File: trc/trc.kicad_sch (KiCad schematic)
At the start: 23 parts, among them J1 PWR, J2 Control, J3 Inverter, J4 BMS, J5 States, J6 Relays, SW1 EXT_FAULT_JUMPER

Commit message: docs(trc): update sheet information
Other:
- title: Pre-Charge -> TSAC Relay Controller
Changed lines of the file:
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@@
   (paper "A4")
   (title_block
-    (title "Pre-Charge")
+    (title "TSAC Relay Controller")
     (date "2023-04-27")
     (rev "2.0.0")

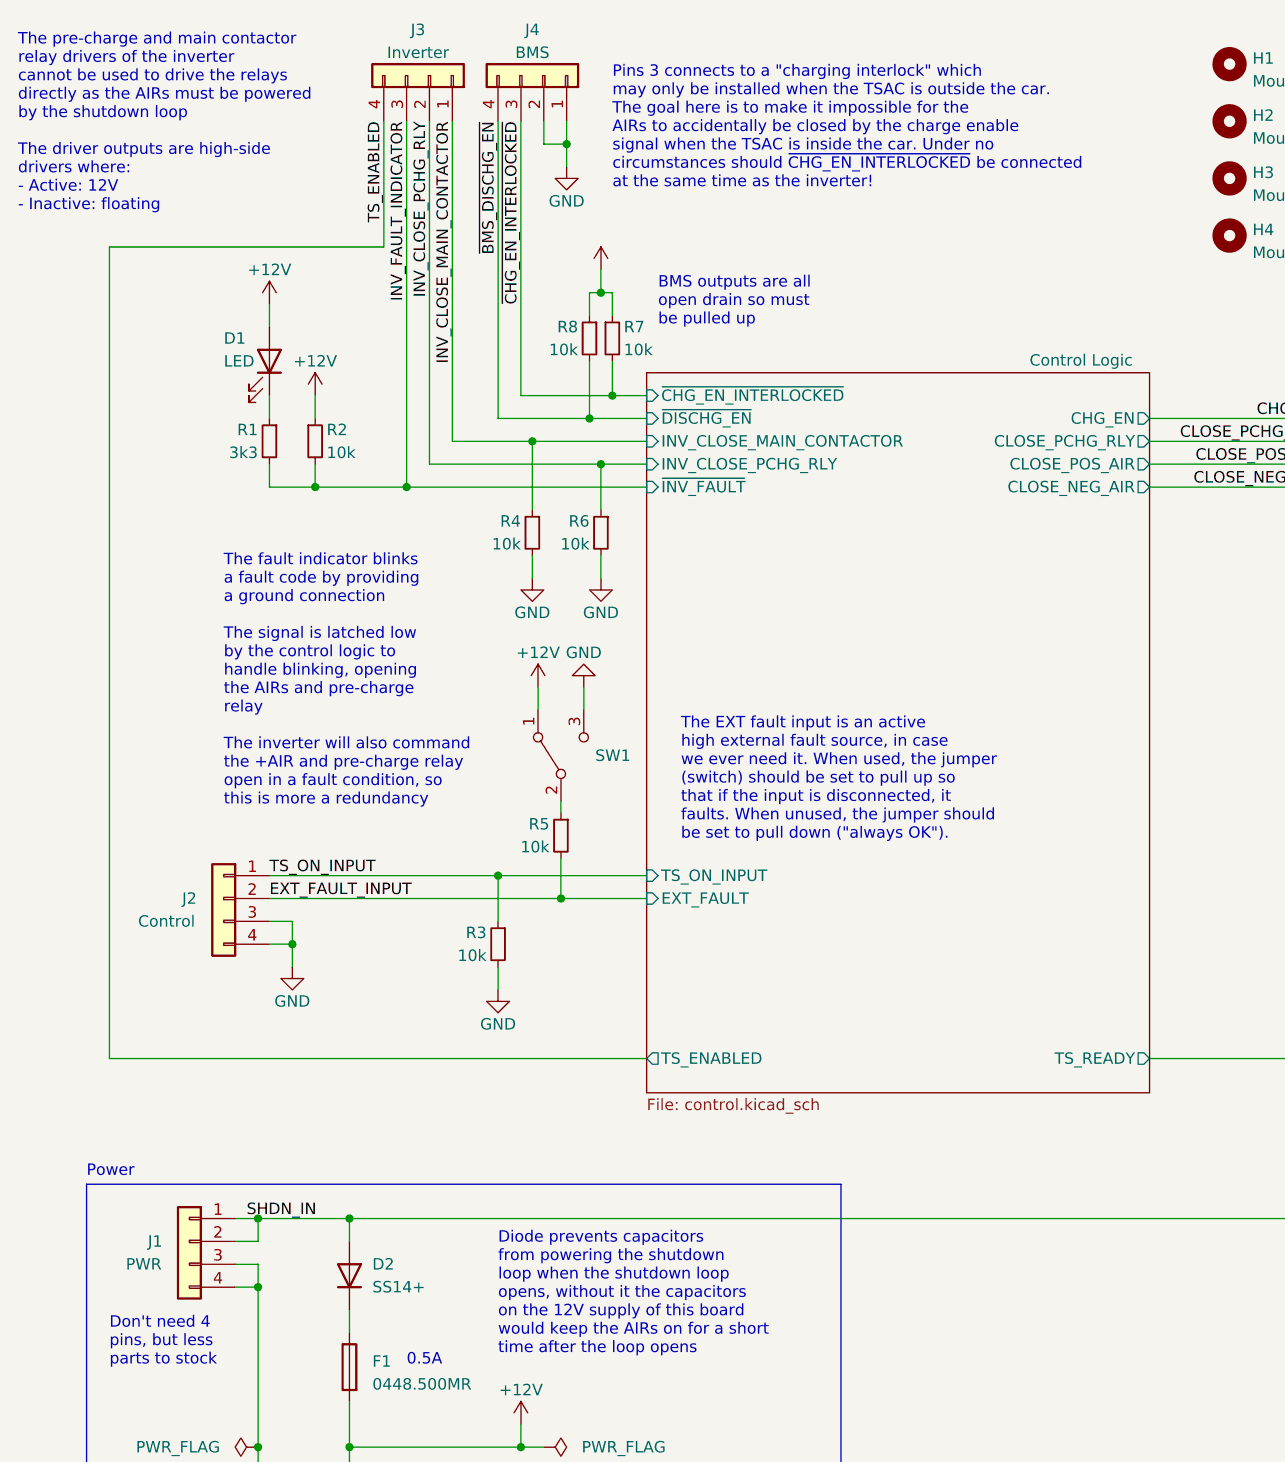
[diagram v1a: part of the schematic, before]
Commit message: feat(trc): swap vertical connectors for horizontal ones
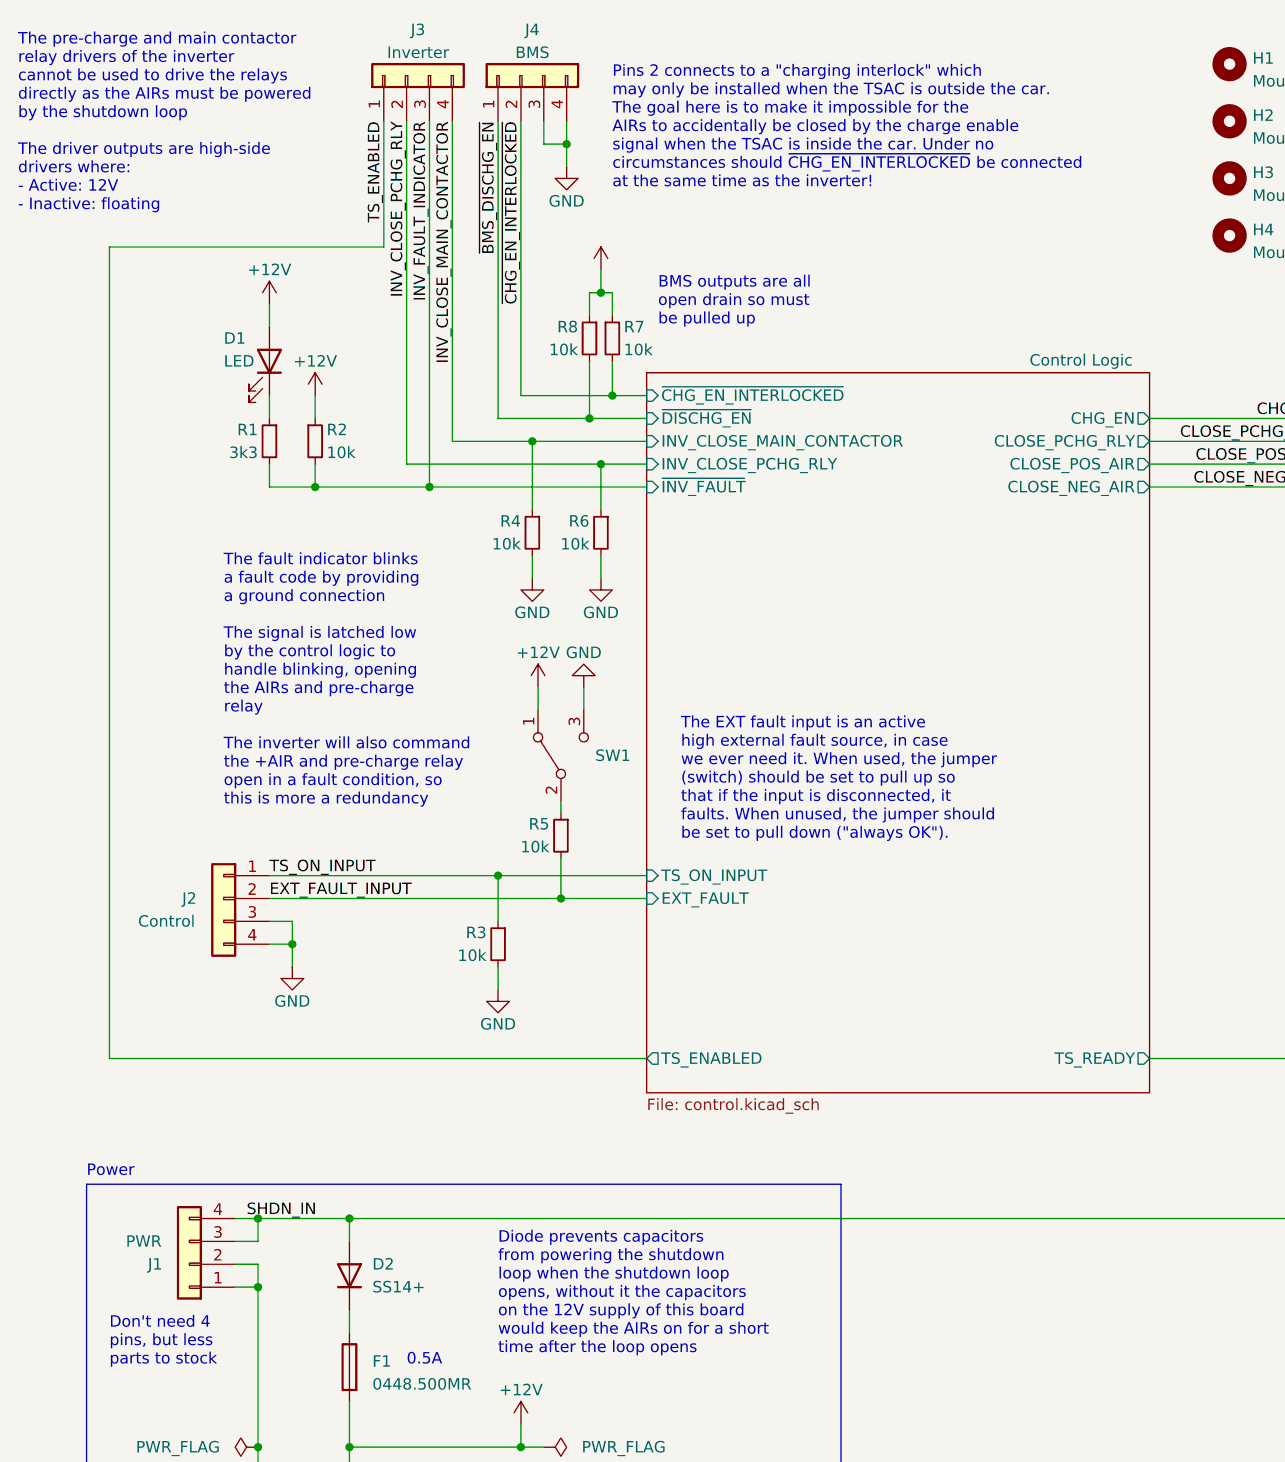
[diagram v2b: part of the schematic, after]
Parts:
- J1, J2, J3, J4: footprint Connector_Molex:Molex_Micro-Fit_3.0_43045-0412_2x02_P3.00mm_Vertical -> Connector_Molex:Molex_Micro-Fit_3.0_43045-0400_2x02_P3.00mm_Horizontal
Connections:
- net GND: now also J1.1 (Pin_1), J1.2 (Pin_2), J4.3 (Pin_3), J4.4 (Pin_4); no longer J1.3 (Pin_3), J1.4 (Pin_4), J4.1 (Pin_1), J4.2 (Pin_2)
- net INV_CLOSE_MAIN_CONTACTOR: now also J3.4 (Pin_4); no longer J3.1 (Pin_1)
- net SHDN_IN: now also J1.3 (Pin_3), J1.4 (Pin_4); no longer J1.1 (Pin_1), J1.2 (Pin_2)
- net TS_ENABLED: now also J3.1 (Pin_1); no longer J3.4 (Pin_4)
- net ~{BMS_DISCHG_EN}: now also J4.1 (Pin_1); no longer J4.4 (Pin_4)
- net ~{CHG_EN_INTERLOCKED}: now also J4.2 (Pin_2); no longer J4.3 (Pin_3)
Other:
- note added: "Pins 2 connects to a "charging interlock" which may only be installed when the TSAC is outside the car. The goal here is to make it impossible for the AIRs to accidentally be closed by the charge enable signal when the TSAC is inside the car. Under no circumstances should ~{CHG_EN_INTERLOCKED} be connected at the same time as the inverter!"
- note removed: "Pins 3 connects to a "charging interlock" which may only be installed when the TSAC is outside the car. The goal here is to make it impossible for the AIRs to accidentally be closed by the charge enable signal when the TSAC is inside the car. Under no circumstances should ~{CHG_EN_INTERLOCKED} be connected at the same time as the inverter!"
- moved on the sheet: J1, J3, J4
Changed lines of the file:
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@@
   (junction (at 81.28 62.23) (diameter 0) (color 0 0 0 0)
   )
+  (junction (at 50.8 148.59) (diameter 0) (color 0 0 0 0)
+  )
+  (junction (at 87.63 59.69) (diameter 0) (color 0 0 0 0)
+  )
+  (junction (at 85.09 29.21) (diameter 0) (color 0 0 0 0)
+  )
+  (junction (at 84.455 113.03) (diameter 0) (color 0 0 0 0)
+  )
+  (junction (at 90.17 57.15) (diameter 0) (color 0 0 0 0)
+  )
+  (junction (at 50.8 173.99) (diameter 0) (color 0 0 0 0)
+  )
+  (junction (at 88.9 45.72) (diameter 0) (color 0 0 0 0)
+  )
+  (junction (at 77.47 110.49) (diameter 0) (color 0 0 0 0)
+  )
   (junction (at 88.9 64.77) (diameter 0) (color 0 0 0 0)
   )
-  (junction (at 50.8 148.59) (diameter 0) (color 0 0 0 0)
-  )
-  (junction (at 87.63 59.69) (diameter 0) (color 0 0 0 0)
-  )
-  (junction (at 85.09 29.21) (diameter 0) (color 0 0 0 0)
-  )
-  (junction (at 84.455 113.03) (diameter 0) (color 0 0 0 0)
-  )
-  (junction (at 90.17 57.15) (diameter 0) (color 0 0 0 0)
-  )
-  (junction (at 50.8 173.99) (diameter 0) (color 0 0 0 0)
-  )
-  (junction (at 88.9 45.72) (diameter 0) (color 0 0 0 0)
-  )
-  (junction (at 77.47 110.49) (diameter 0) (color 0 0 0 0)
-  )
   (junction (at 80.01 173.99) (diameter 0) (color 0 0 0 0)
   )
   (junction (at 57.15 67.31) (diameter 0) (color 0 0 0 0)
   )
-  (junction (at 67.31 67.31) (diameter 0) (color 0 0 0 0)
+  (junction (at 69.85 67.31) (diameter 0) (color 0 0 0 0)
   )
   (junction (at 60.96 173.99) (diameter 0) (color 0 0 0 0)
@@
     (stroke (width 0) (type default))
   )
-  (wire (pts (xy 57.15 67.31) (xy 67.31 67.31))
-    (stroke (width 0) (type default))
-  )
   (wire (pts (xy 87.63 45.72) (xy 87.63 48.26))
     (stroke (width 0) (type default))
@@
     (stroke (width 0) (type default))
   )
-  (wire (pts (xy 69.85 26.67) (xy 69.85 64.77))
+  (wire (pts (xy 69.85 26.67) (xy 69.85 67.31))
     (stroke (width 0) (type default))
   )
@@
     (stroke (width 0) (type default))
   )
+  (wire (pts (xy 64.77 40.64) (xy 34.29 40.64))
+    (stroke (width 0) (type default))
+  )
   (wire (pts (xy 171.45 130.81) (xy 149.86 130.81))
     (stroke (width 0) (type default))
@@
     (stroke (width 0) (type default))
   )
-  (wire (pts (xy 34.29 40.64) (xy 64.77 40.64))
-    (stroke (width 0) (type default))
-  )
   (wire (pts (xy 88.9 43.18) (xy 88.9 45.72))
     (stroke (width 0) (type default))
@@
     (stroke (width 0) (type default))
   )
-  (wire (pts (xy 67.31 26.67) (xy 67.31 67.31))
-    (stroke (width 0) (type default))
-  )
   (wire (pts (xy 87.63 45.72) (xy 88.9 45.72))
     (stroke (width 0) (type default))
   )
+  (wire (pts (xy 67.31 64.77) (xy 67.31 26.67))
+    (stroke (width 0) (type default))
+  )
   (bus (pts (xy 171.45 69.85) (xy 171.45 85.09))
     (stroke (width 0) (type default))
@@
     (stroke (width 0) (type default))
   )
+  (wire (pts (xy 88.9 64.77) (xy 67.31 64.77))
+    (stroke (width 0) (type default))
+  )
   (bus (pts (xy 171.45 67.31) (xy 171.45 64.77))
     (stroke (width 0) (type default))
   )
-  (wire (pts (xy 67.31 67.31) (xy 93.98 67.31))
-    (stroke (width 0) (type default))
-  )
   (polyline (pts (xy 115.57 194.31) (xy 115.57 144.78))
     (stroke (width 0) (type default))
@@
     (stroke (width 0) (type default))
   )
+  (wire (pts (xy 64.77 26.67) (xy 64.77 40.64))
+    (stroke (width 0) (type default))
+  )
   (wire (pts (xy 77.47 110.49) (xy 93.98 110.49))
     (stroke (width 0) (type default))
@@
     (stroke (width 0) (type default))
   )
-  (wire (pts (xy 64.77 26.67) (xy 64.77 40.64))
+  (wire (pts (xy 69.85 67.31) (xy 93.98 67.31))
     (stroke (width 0) (type default))
   )
@@
     (stroke (width 0) (type default))
   )
-  (wire (pts (xy 88.9 64.77) (xy 69.85 64.77))
-    (stroke (width 0) (type default))
-  )
   (wire (pts (xy 149.86 62.23) (xy 168.91 62.23))
     (stroke (width 0) (type default))
@@
   )
   (wire (pts (xy 88.9 45.72) (xy 90.17 45.72))
+    (stroke (width 0) (type default))
+  )
+  (wire (pts (xy 57.15 67.31) (xy 69.85 67.31))
     (stroke (width 0) (type default))
   )
@@
     (effects (font (size 1.27 1.27)) (justify left bottom))
   )
-  (text "Pins 3 connects to a \"charging interlock\" which \nmay only be installed when the TSAC is outside the car.\nThe goal here is to make it impossible for the\nAIRs to accidentally be closed by the charge enable\nsignal when the TSAC is inside the car. Under no\ncircumstances should ~{CHG_EN_INTERLOCKED} be connected\nat the same time as the inverter!"
+  (text "Pins 2 connects to a \"charging interlock\" which \nmay only be installed when the TSAC is outside the car.\nThe goal here is to make it impossible for the\nAIRs to accidentally be closed by the charge enable\nsignal when the TSAC is inside the car. Under no\ncircumstances should ~{CHG_EN_INTERLOCKED} be connected\nat the same time as the inverter!"
     (at 90.17 34.29 0)
     (effects (font (size 1.27 1.27)) (justify left bottom))
@@
     (effects (font (size 1.27 1.27)) (justify left bottom))
   )
-  (label "INV_FAULT_INDICATOR" (at 67.31 26.67 270) (fields_autoplaced)
+  (label "INV_FAULT_INDICATOR" (at 69.85 26.67 270) (fields_autoplaced)
     (effects (font (size 1.27 1.27)) (justify right bottom))
   )
@@
     (effects (font (size 1.27 1.27)) (justify right bottom))
   )
-  (label "INV_CLOSE_PCHG_RLY" (at 69.85 26.67 270) (fields_autoplaced)
+  (label "INV_CLOSE_PCHG_RLY" (at 67.31 26.67 270) (fields_autoplaced)
     (effects (font (size 1.27 1.27)) (justify right bottom))
   )
@@
     )
   )
-  (symbol (lib_id "Connector_Generic:Conn_01x04") (at 69.85 21.59 270) (mirror x) (unit 1)
+  (symbol (lib_id "Connector_Generic:Conn_01x04") (at 67.31 21.59 90) (unit 1)
     (in_bom yes) (on_board yes) (dnp no)
     (property "Reference" "J3" (at 68.58 16.51 90)
@@
       (effects (font (size 1.27 1.27)))
     )
-    (property "Footprint" "Connector_Molex:Molex_Micro-Fit_3.0_43045-0412_2x02_P3.00mm_Vertical" (at 69.85 21.59 0)
-      (effects (font (size 1.27 1.27)) hide)
-    )
-    (property "Datasheet" "~" (at 69.85 21.59 0)
+    (property "Footprint" "Connector_Molex:Molex_Micro-Fit_3.0_43045-0400_2x02_P3.00mm_Horizontal" (at 67.31 21.59 0)
+      (effects (font (size 1.27 1.27)) hide)
+    )
+    (property "Datasheet" "~" (at 67.31 21.59 0)
       (effects (font (size 1.27 1.27)) hide)
     )
@@
     )
   )
-  (symbol (lib_id "Connector_Generic:Conn_01x04") (at 82.55 21.59 270) (mirror x) (unit 1)
+  (symbol (lib_id "Connector_Generic:Conn_01x04") (at 80.01 21.59 90) (unit 1)
     (in_bom yes) (on_board yes) (dnp no)
     (property "Reference" "J4" (at 81.28 16.51 90)
@@
       (effects (font (size 1.27 1.27)))
     )
-    (property "Footprint" "Connector_Molex:Molex_Micro-Fit_3.0_43045-0412_2x02_P3.00mm_Vertical" (at 82.55 21.59 0)
-      (effects (font (size 1.27 1.27)) hide)
-    )
-    (property "Datasheet" "~" (at 82.55 21.59 0)
+    (property "Footprint" "Connector_Molex:Molex_Micro-Fit_3.0_43045-0400_2x02_P3.00mm_Horizontal" (at 80.01 21.59 0)
+      (effects (font (size 1.27 1.27)) hide)
+    )
+    (property "Datasheet" "~" (at 80.01 21.59 0)
       (effects (font (size 1.27 1.27)) hide)
     )
@@
       (effects (font (size 1.27 1.27)))
     )
-    (property "Footprint" "Connector_Molex:Molex_Micro-Fit_3.0_43045-0412_2x02_P3.00mm_Vertical" (at 46.99 113.03 0)
+    (property "Footprint" "Connector_Molex:Molex_Micro-Fit_3.0_43045-0400_2x02_P3.00mm_Horizontal" (at 46.99 113.03 0)
       (effects (font (size 1.27 1.27)) hide)
     )
@@
     )
   )
-  (symbol (lib_id "Connector_Generic:Conn_01x04") (at 43.18 151.13 0) (mirror y) (unit 1)
-    (in_bom yes) (on_board yes) (dnp no)
-    (property "Reference" "J1" (at 39.37 151.13 0)
-      (effects (font (size 1.27 1.27)))
-    )
-    (property "Value" "PWR" (at 38.1 153.67 0)
-      (effects (font (size 1.27 1.27)))
-    )
-    (property "Footprint" "Connector_Molex:Molex_Micro-Fit_3.0_43045-0412_2x02_P3.00mm_Vertical" (at 43.18 151.13 0)
-      (effects (font (size 1.27 1.27)) hide)
-    )
-    (property "Datasheet" "~" (at 43.18 151.13 0)
-      (effects (font (size 1.27 1.27)) hide)
-    )
+  (symbol (lib_id "Connector_Generic:Conn_01x04") (at 43.18 153.67 180) (unit 1)
+    (in_bom yes) (on_board yes) (dnp no)
+    (property "Reference" "J1" (at 39.37 153.67 0)
+      (effects (font (size 1.27 1.27)))
+    )
+    (property "Value" "PWR" (at 38.1 151.13 0)
+      (effects (font (size 1.27 1.27)))
+    )
+    (property "Footprint" "Connector_Molex:Molex_Micro-Fit_3.0_43045-0400_2x02_P3.00mm_Horizontal" (at 43.18 153.67 0)
+      (effects (font (size 1.27 1.27)) hide)
+    )
+    (property "Datasheet" "~" (at 43.18 153.67 0)
+      (effects (font (size 1.27 1.27)) hide)
+    )

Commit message: Added TODO tasks
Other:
- note added: "TRC TODO: - Filters - Test stability of 12V - Ground return path for whole shutdown loop?"
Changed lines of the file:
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@@
     (effects (font (size 1.27 1.27)) (justify left bottom))
+  )
+  (text "TRC TODO:\n- Filters\n- Test stability of 12V\n- Ground return path for whole shutdown loop?"
+    (at 223.52 27.305 0)
+    (effects (font (size 1.27 1.27) (color 255 0 0 1)) (justify left bottom))
   )
   (text "Pins 2 connects to a \"charging interlock\" which \nmay only be installed when the TSAC is outside the car.\nThe goal here is to make it impossible for the\nAIRs to accidentally be closed by the charge enable\nsignal when the TSAC is inside the car. Under no\ncircumstances should ~{CHG_EN_INTERLOCKED} be connected\nat the same time as the inverter!"
